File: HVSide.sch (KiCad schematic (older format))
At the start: 50 parts, among them J11 CONN_2X2, J17 HV, J18 CONN_1X2, J19 CONN_1X2, J4 CONN_2X2, U10 DCDC_ISO_5V_ISO, U15 CD4082, U16 ADCMP350, U19 TCMT1103, U23 CD4072BPW, U24 LTC6259, U26 TCMT1103, U27 DCDC_ISO_5V, U28 MIC5365-3.3YC5, U29 Si8900, U30 MAX14878AWA+, U7 ADCMP354

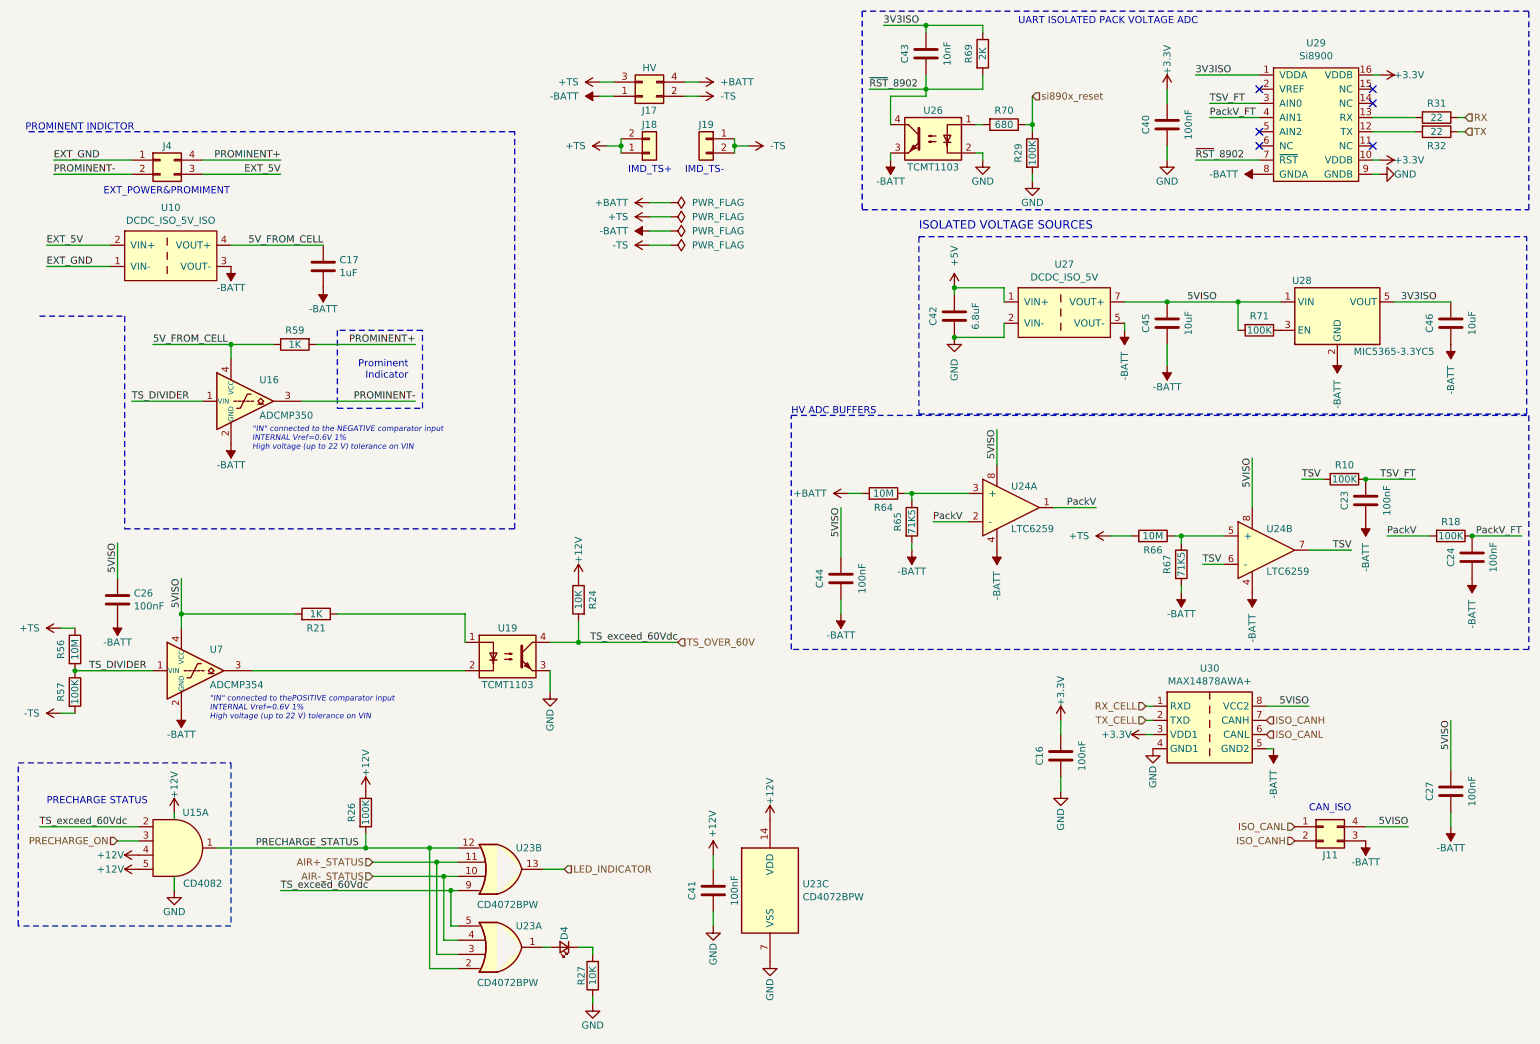
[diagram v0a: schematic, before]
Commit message: added a lot of annotations and readability in the schematic, not complete
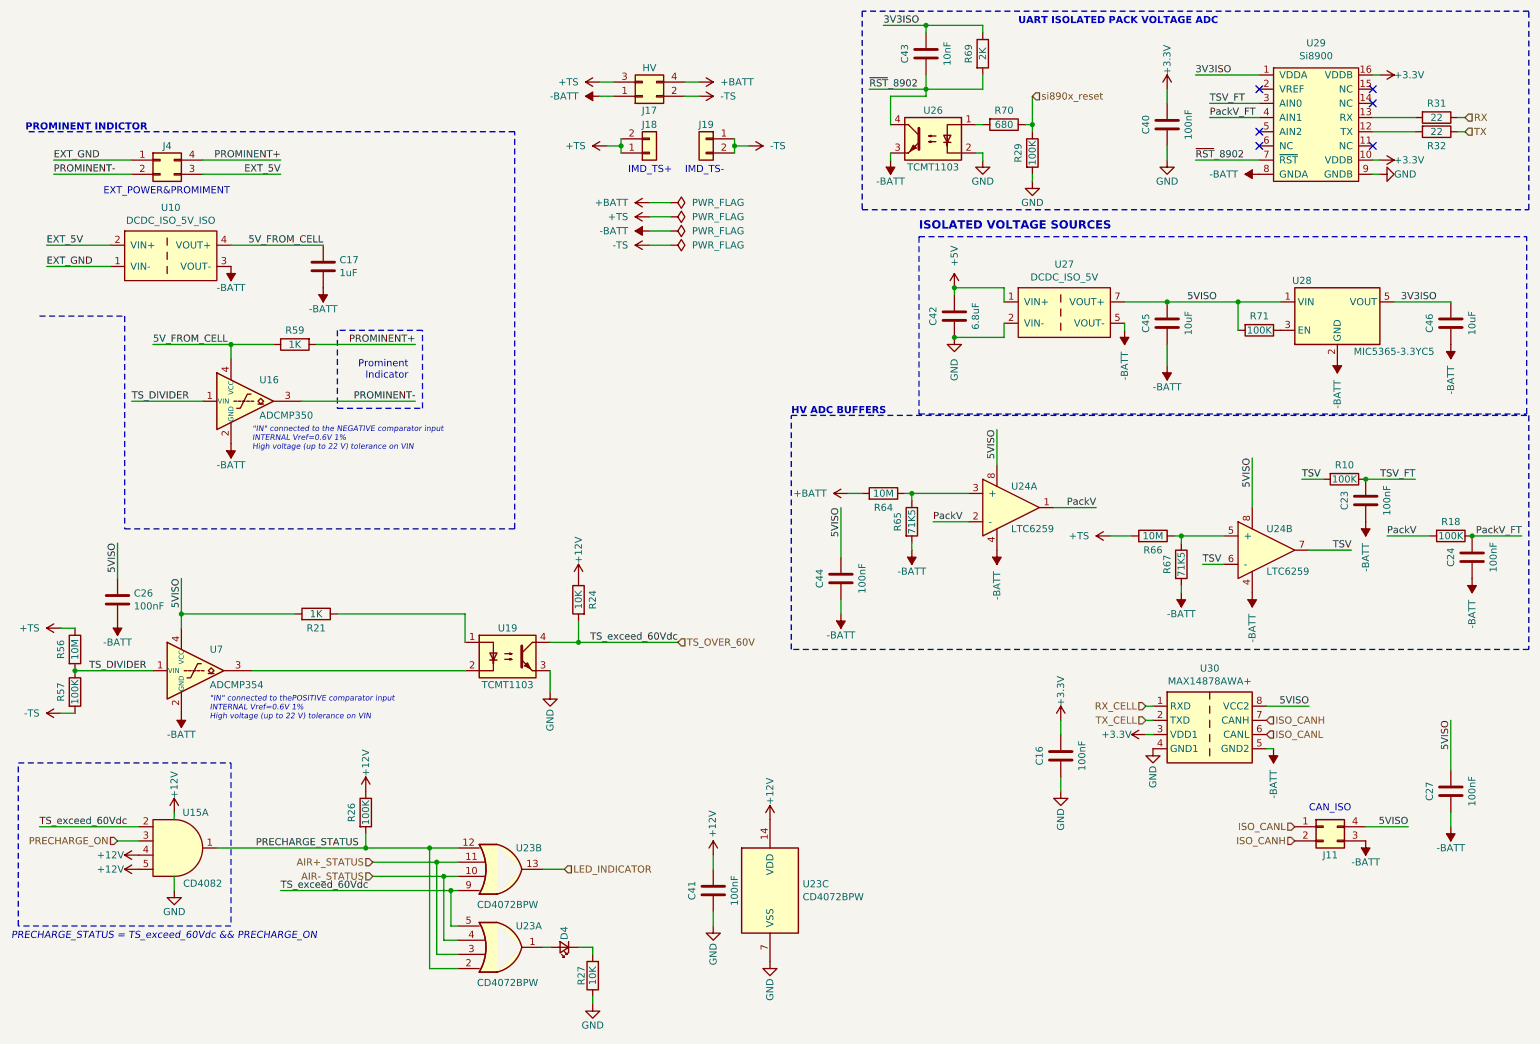
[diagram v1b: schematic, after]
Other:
- note added: "PRECHARGE_STATUS = TS_exceed_60Vdc && PRECHARGE_ON\n"
- note removed: "PRECHARGE STATUS"
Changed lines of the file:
@@
 	0    1    1    0
 $EndComp
-Text Notes 7600 600  0    50   ~ 0
+Text Notes 7600 600  0    50   ~ 10
 UART ISOLATED PACK VOLTAGE ADC
 $Comp
@@
 Wire Notes Line
 	6900 2090 6900 3340
-Text Notes 6900 2050 0    59   ~ 0
+Text Notes 6900 2050 0    59   ~ 12
 ISOLATED VOLTAGE SOURCES
 Wire Notes Line
@@
 Wire Wire Line
 	7000 4100 7250 4100
-Text Notes 6000 3350 0    50   ~ 0
+Text Notes 6000 3350 0    50   ~ 10
 HV ADC BUFFERS
 $Comp
@@
 	-1   0    0    1
 $EndComp
-Text Notes 750  6100 0    50   ~ 0
-PRECHARGE STATUS
+Text Notes 500  7050 0    50   Italic 0
+PRECHARGE_STATUS = TS_exceed_60Vdc && PRECHARGE_ON\n
 Text HLabel 1250 6350 0    50   Input ~ 0
 PRECHARGE_ON
@@
 Wire Notes Line
 	4050 1350 600  1350
-Text Notes 600  1350 0    50   ~ 0
+Text Notes 600  1350 0    50   ~ 10
 PROMINENT INDICTOR
 $Comp

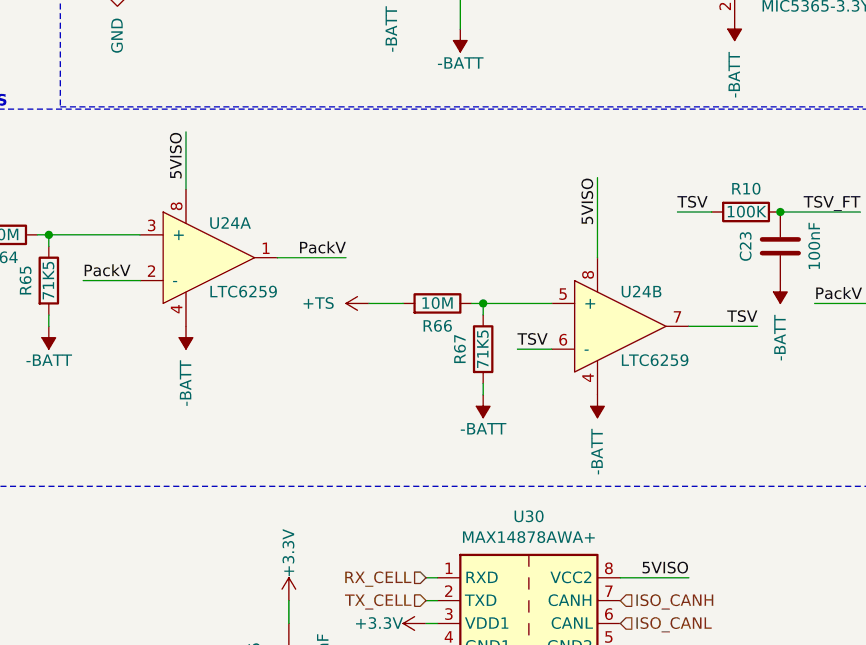
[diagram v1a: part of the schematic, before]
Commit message: updated to new components as per v1.0.5
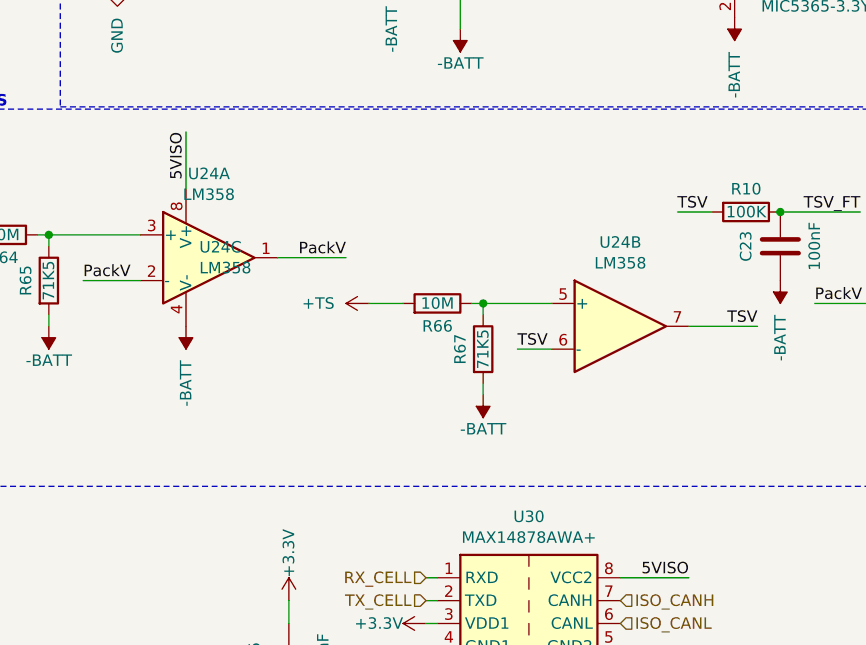
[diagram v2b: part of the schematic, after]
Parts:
- removed U24: LTC6259, Package_TO_SOT_SMD:TSOT-23-8, symbol MainBoard:LTC6259
- added U24: LM358, Package_TO_SOT_SMD:TSOT-23-8, symbol Amplifier_Operational:LM358
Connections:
- net -BATT: now also U24.4 (V-)
- net 5VISO: now also U24.8 (V+)
- net PackV: now also U24.1, U24.2 (-)
- net TSV: now also U24.6 (-), U24.7
- net at R64.1, R65.1: now also U24.3 (+)
- net at R66.1, R67.1: now also U24.5 (+)
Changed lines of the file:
@@
 Wire Wire Line
 	6850 3900 6850 3950
-$Comp
-L MainBoard:LTC6259 U24
-U 1 1 5E18413A
-P 7500 4000
-F 0 "U24" H 7550 4150 50  0000 L CNN
-F 1 "LTC6259" H 7550 3850 50  0000 L CNN
-F 2 "Package_TO_SOT_SMD:TSOT-23-8" H 7550 3750 50  0001 L CNN
-F 3 "www.analog.com/media/en/technical-documentation/data-sheets/6258960fa.pdf" H 7500 3950 50  0001 C CNN
-F 4 "https://www.mouser.it/ProductDetail/Analog-Devices/LTC6259ITS8TRPBF?qs=u4fy%2FsgLU9NqjanGCTJjzA%3D%3D" H 7500 4000 50  0001 C CNN "Mouser"
-	1    7500 4000
-	1    0    0    -1
-$EndComp
 Wire Wire Line
 	8150 4000 7850 4000
@@
 Wire Wire Line
 	9650 4300 9950 4300
-$Comp
-L power:-BATT #PWR0206
-U 1 1 5E1CC103
-P 9250 4600
-F 0 "#PWR0206" H 9250 4450 50  0001 C CNN
-F 1 "-BATT" V 9250 4850 50  0000 C CNN
-F 2 "" H 9250 4600 50  0001 C CNN
-F 3 "" H 9250 4600 50  0001 C CNN
-	1    9250 4600
-	-1   0    0    1
-$EndComp
-$Comp
-L MainBoard:LTC6259 U24
-U 2 1 5E184D16
-P 9300 4300
-F 0 "U24" H 9350 4450 50  0000 L CNN
-F 1 "LTC6259" H 9350 4150 50  0000 L CNN
-F 2 "Package_TO_SOT_SMD:TSOT-23-8" H 9350 4050 50  0001 L CNN
-F 3 "www.analog.com/media/en/technical-documentation/data-sheets/6258960fa.pdf" H 9300 4250 50  0001 C CNN
-F 4 "https://www.mouser.it/ProductDetail/Analog-Devices/LTC6259ITS8TRPBF?qs=u4fy%2FsgLU9NqjanGCTJjzA%3D%3D" H 9300 4300 50  0001 C CNN "Mouser"
-	2    9300 4300
-	1    0    0    -1
-$EndComp
 Wire Wire Line
 	8700 4200 8750 4200
@@
 NoConn ~ 9300 1050
 Wire Wire Line
-	9250 4000 9250 3650
-Wire Wire Line
 	7450 3450 7450 3700
-Text Label 9250 3650 3    50   ~ 0
-5VISO
 Text Label 7450 3450 3    50   ~ 0
 5VISO
@@
 	3450 6400 3650 6400
 Connection ~ 3450 6400
+$Comp
+L Amplifier_Operational:LM358 U24
+U 1 1 5FD8D2B7
+P 7550 4000
+F 0 "U24" H 7550 4367 50  0000 C CNN
+F 1 "LM358" H 7550 4276 50  0000 C CNN
+F 2 "Package_TO_SOT_SMD:TSOT-23-8" H 7550 4000 50  0001 C CNN
+F 3 "http://www.ti.com/lit/ds/symlink/lm2904-n.pdf" H 7550 4000 50  0001 C CNN
+	1    7550 4000
+	1    0    0    -1
+$EndComp
+$Comp
+L Amplifier_Operational:LM358 U24
+U 2 1 5FD922D9
+P 9350 4300
+F 0 "U24" H 9350 4667 50  0000 C CNN
+F 1 "LM358" H 9350 4576 50  0000 C CNN
+F 2 "Package_TO_SOT_SMD:TSOT-23-8" H 9350 4300 50  0001 C CNN
+F 3 "http://www.ti.com/lit/ds/symlink/lm2904-n.pdf" H 9350 4300 50  0001 C CNN
+	2    9350 4300
+	1    0    0    -1
+$EndComp
+$Comp
+L Amplifier_Operational:LM358 U24
+U 3 1 5FD954EF
+P 7550 4000
+F 0 "U24" H 7508 4046 50  0000 L CNN
+F 1 "LM358" H 7508 3955 50  0000 L CNN
+F 2 "Package_TO_SOT_SMD:TSOT-23-8" H 7550 4000 50  0001 C CNN
+F 3 "http://www.ti.com/lit/ds/symlink/lm2904-n.pdf" H 7550 4000 50  0001 C CNN
+	3    7550 4000
+	1    0    0    -1
+$EndComp
 $EndSCHEMATC
